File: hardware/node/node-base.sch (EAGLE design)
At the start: 19 parts, among them U1 INA322_DGK_8, U2 LMV551_DBV_5

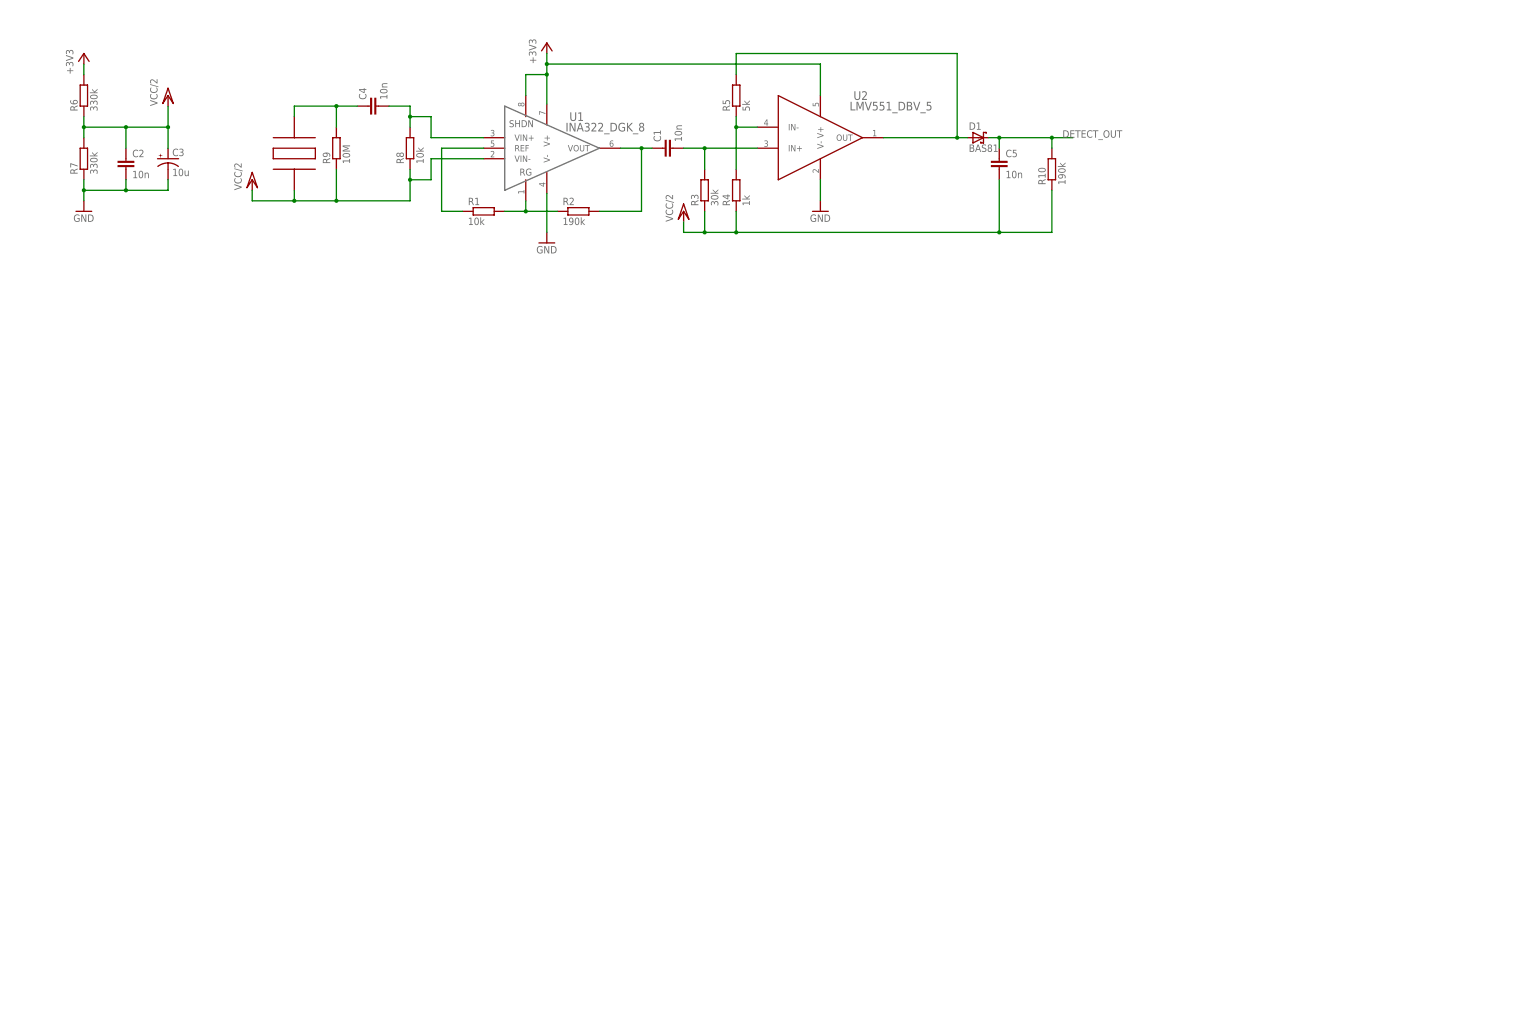
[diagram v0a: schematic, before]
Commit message: NODEHW: Added MCU power
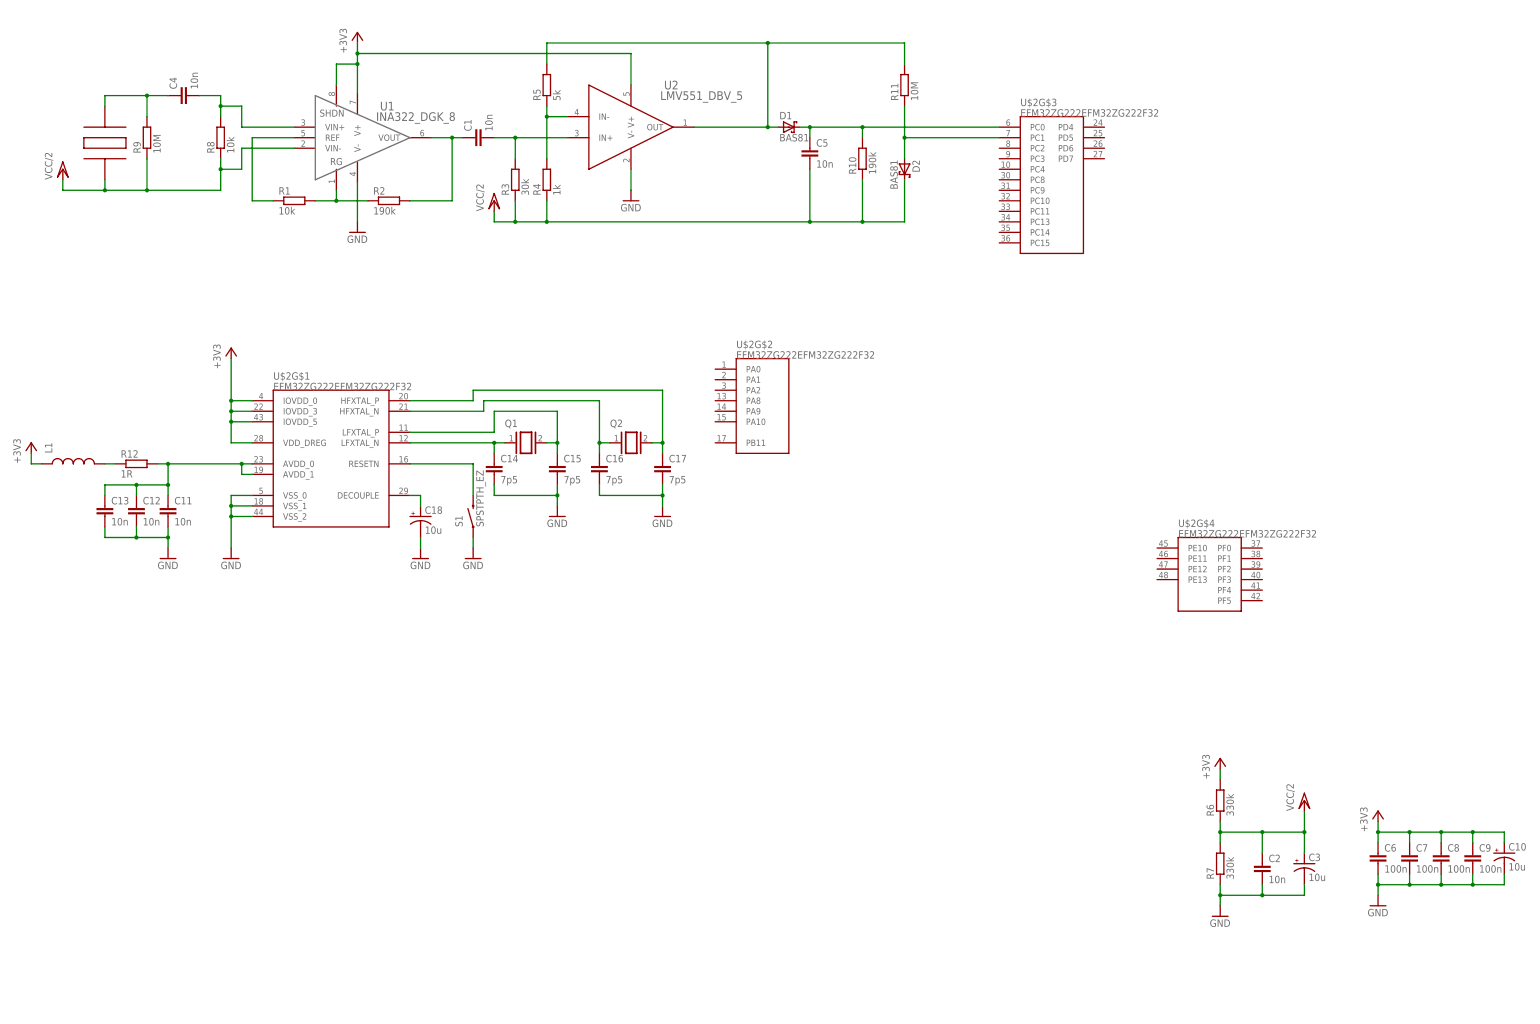
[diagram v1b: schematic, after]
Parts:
- added C10, C18: 10u, SparkFun-Capacitors:CAP_POLPTH2
- added C11, C12, C13: 10n, SparkFun-Capacitors:CAPPTH
- added C14, C15, C16, C17: 7p5, SparkFun-Capacitors:CAPPTH
- added C6, C7, C8, C9: 100n, SparkFun-Capacitors:CAPPTH
- added D2: BAS81, diode:SCHOTTKY-DIODECB417-15
- added L1: (no value), SparkFun-Passives:INDUCTOR0805
- added Q1, Q2: (no value), special:XTAL/S
- added R11: 10M, resistor:R-EU_0309/12
- added R12: 1R, resistor:R-EU_0309/12
- added S1: SPSTPTH_EZ, SparkFun-Electromechanical:SPSTPTH_EZ
- added U$2: EFM32ZG222EFM32ZG222F32, FullyCustom:EFM32ZG222EFM32ZG222F32
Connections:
- new net N$12: S1.2, U$2G$1.RESETN
- new net N$14: C14.1, Q1.1, U$2G$1.LFXTAL_N
- new net N$16: C15.1, Q1.2, U$2G$1.LFXTAL_P
- new net N$17: C16.1, Q2.1, U$2G$1.HFXTAL_N
- new net N$18: C17.1, Q2.2, U$2G$1.HFXTAL_P
- new net N$23: C18.+, U$2G$1.DECOUPLE
- new net N$3: D2.A, R11.1, U$2G$3.PC1
- new net N$6: L1.2, R12.1
- new net N$8: C11.1, C12.1, C13.1, R12.2, U$2G$1.AVDD_0, U$2G$1.AVDD_1
- net +3V3: now also C10.+, C6.1, C7.1, C8.1, C9.1, L1.1, U$2G$1.IOVDD_0, U$2G$1.IOVDD_3, U$2G$1.IOVDD_5, U$2G$1.VDD_DREG
- net DETECT_OUT: now also U$2G$3.PC0
- net GND: now also C10.-, C11.2, C12.2, C13.2, C14.2, C15.2, C16.2, C17.2, C18.-, C6.2, C7.2, C8.2, C9.2, S1.1, U$2G$1.VSS_0, U$2G$1.VSS_1, U$2G$1.VSS_2
- net N$2: now also R11.2
- net VCC/2: now also D2.C
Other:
- moved on the sheet: C1, C2, C3, C4, C5, D1, R1, R10, R2, R3, R4, R5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

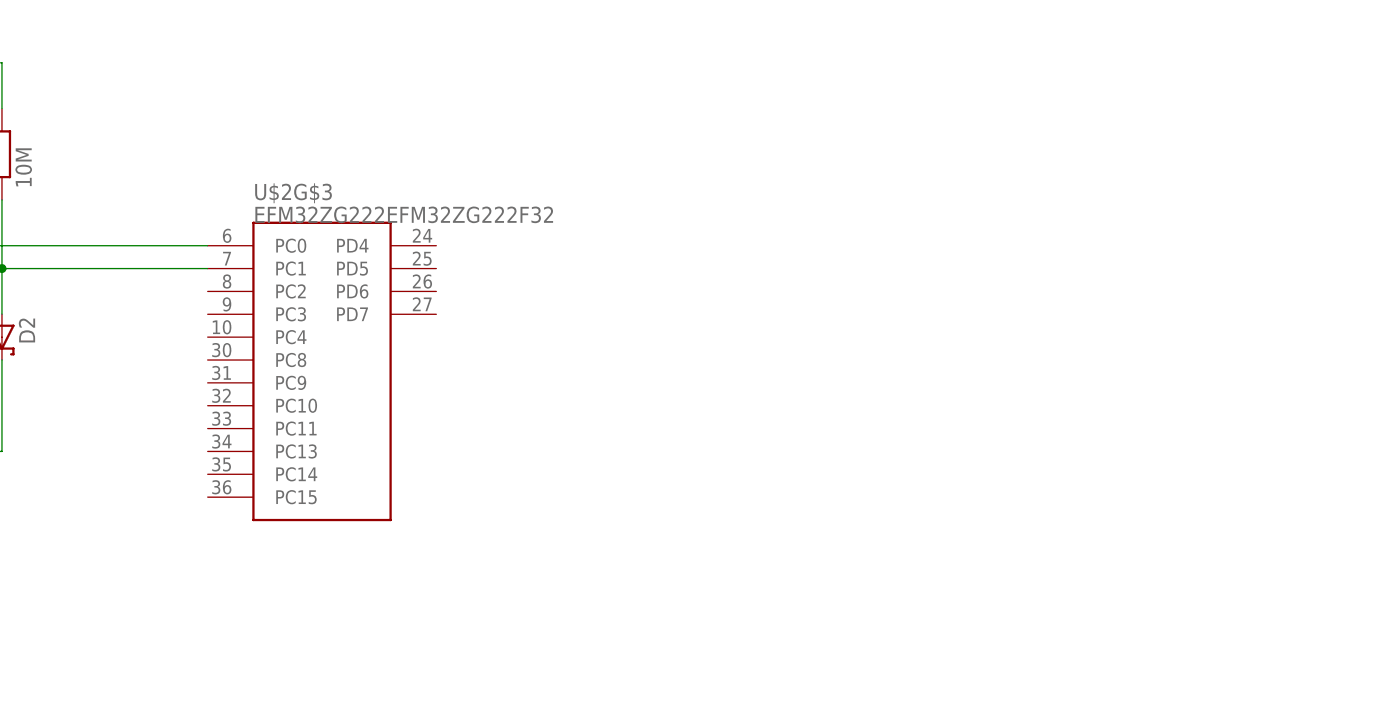
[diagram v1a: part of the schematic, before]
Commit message: NODE: Added radio
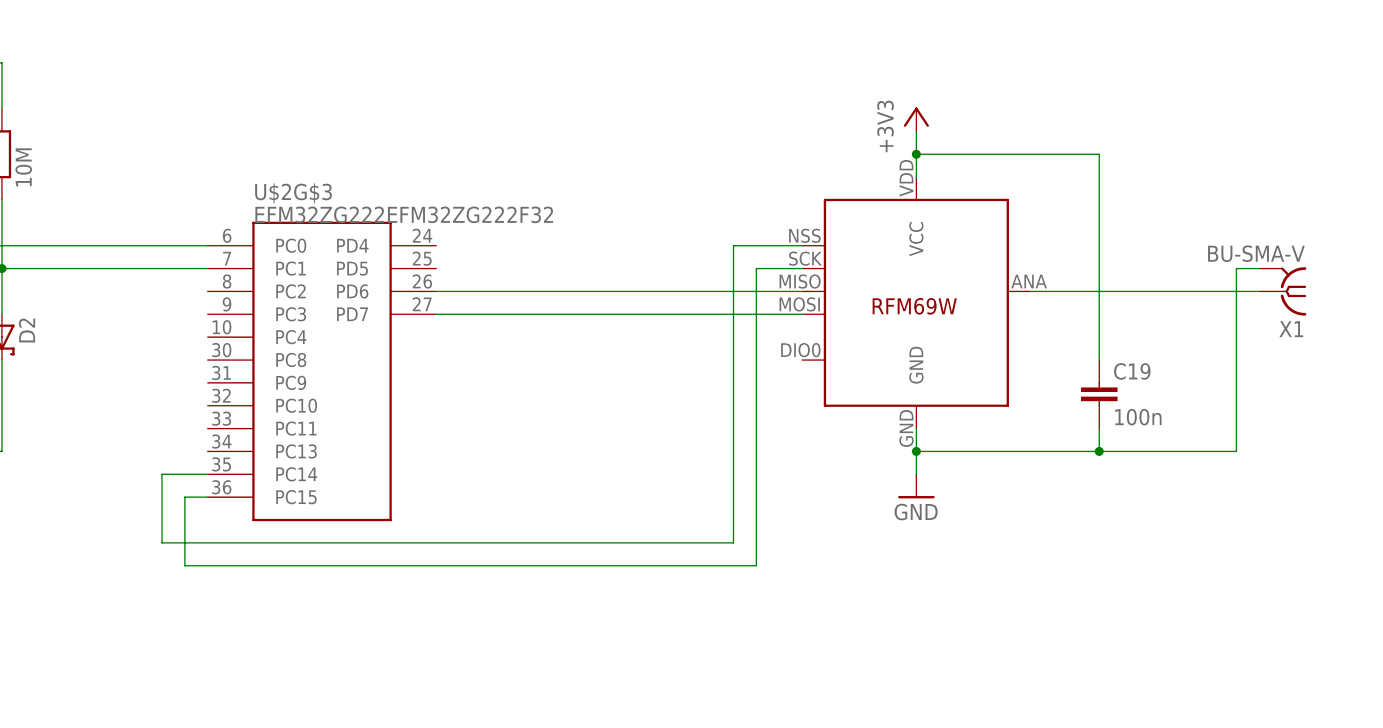
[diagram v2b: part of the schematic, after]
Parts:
- added C19: 100n, SparkFun-Capacitors:CAPPTH
- added U$3: RFM69, Moteino:RFM69
- added X1: BU-SMA-V, con-coax:BU-SMA-V
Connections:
- new net N$13: U$2G$3.PD6, U$3.MISO
- new net N$15: U$2G$3.PD7, U$3.MOSI
- new net N$19: U$2G$3.PC14, U$3.SEL
- new net N$20: U$2G$3.PC15, U$3.SCK
- new net N$22: U$3.ANT, X1.1
- net +3V3: now also C19.1, U$3.VCC
- net GND: now also C19.2, U$3.GND, X1.2
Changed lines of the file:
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@@
 <grid distance="0.1" unitdist="inch" unit="inch" style="lines" multiple="1" display="no" altdistance="0.01" altunitdist="inch" altunit="inch"/>
 <layers>
-<layer number="1" name="Top" color="4" fill="1" visible="yes" active="no"/>
-<layer number="16" name="Bottom" color="1" fill="1" visible="yes" active="no"/>
-<layer number="17" name="Pads" color="2" fill="1" visible="yes" active="no"/>
-<layer number="18" name="Vias" color="2" fill="1" visible="yes" active="no"/>
-<layer number="19" name="Unrouted" color="6" fill="1" visible="yes" active="no"/>
-<layer number="20" name="Dimension" color="15" fill="1" visible="yes" active="no"/>
-<layer number="21" name="tPlace" color="7" fill="1" visible="yes" active="no"/>
-<layer number="22" name="bPlace" color="7" fill="1" visible="yes" active="no"/>
-<layer number="23" name="tOrigins" color="15" fill="1" visible="yes" active="no"/>
-<layer number="24" name="bOrigins" color="15" fill="1" visible="yes" active="no"/>
-<layer number="25" name="tNames" color="7" fill="1" visible="yes" active="no"/>
-<layer number="26" name="bNames" color="7" fill="1" visible="yes" active="no"/>
-<layer number="27" name="tValues" color="7" fill="1" visible="yes" active="no"/>
-<layer number="28" name="bValues" color="7" fill="1" visible="yes" active="no"/>
+<layer number="1" name="Top" color="4" fill="1" visible="no" active="no"/>
+<layer number="16" name="Bottom" color="1" fill="1" visible="no" active="no"/>
+<layer number="17" name="Pads" color="2" fill="1" visible="no" active="no"/>
+<layer number="18" name="Vias" color="2" fill="1" visible="no" active="no"/>
+<layer number="19" name="Unrouted" color="6" fill="1" visible="no" active="no"/>
+<layer number="20" name="Dimension" color="15" fill="1" visible="no" active="no"/>
+<layer number="21" name="tPlace" color="7" fill="1" visible="no" active="no"/>
+<layer number="22" name="bPlace" color="7" fill="1" visible="no" active="no"/>
+<layer number="23" name="tOrigins" color="15" fill="1" visible="no" active="no"/>
+<layer number="24" name="bOrigins" color="15" fill="1" visible="no" active="no"/>
+<layer number="25" name="tNames" color="7" fill="1" visible="no" active="no"/>
+<layer number="26" name="bNames" color="7" fill="1" visible="no" active="no"/>
+<layer number="27" name="tValues" color="7" fill="1" visible="no" active="no"/>
+<layer number="28" name="bValues" color="7" fill="1" visible="no" active="no"/>
 <layer number="29" name="tStop" color="7" fill="3" visible="no" active="no"/>
 <layer number="30" name="bStop" color="7" fill="6" visible="no" active="no"/>
@@
 <layer number="35" name="tGlue" color="7" fill="4" visible="no" active="no"/>
 <layer number="36" name="bGlue" color="7" fill="5" visible="no" active="no"/>
-<layer number="37" name="tTest" color="7" fill="1" visible="yes" active="no"/>
-<layer number="38" name="bTest" color="7" fill="1" visible="yes" active="no"/>
+<layer number="37" name="tTest" color="7" fill="1" visible="no" active="no"/>
+<layer number="38" name="bTest" color="7" fill="1" visible="no" active="no"/>
 <layer number="39" name="tKeepout" color="4" fill="11" visible="no" active="no"/>
 <layer number="40" name="bKeepout" color="1" fill="11" visible="no" active="no"/>
@@
 <layer number="44" name="Drills" color="7" fill="1" visible="no" active="no"/>
 <layer number="45" name="Holes" color="7" fill="1" visible="no" active="no"/>
-<layer number="46" name="Milling" color="3" fill="1" visible="yes" active="no"/>
-<layer number="47" name="Measures" color="7" fill="1" visible="yes" active="no"/>
-<layer number="48" name="Document" color="7" fill="1" visible="yes" active="no"/>
-<layer number="49" name="Reference" color="7" fill="1" visible="yes" active="no"/>
-<layer number="50" name="dxf" color="7" fill="1" visible="yes" active="no"/>
-<layer number="51" name="tDocu" color="7" fill="1" visible="yes" active="no"/>
-<layer number="52" name="bDocu" color="7" fill="1" visible="yes" active="no"/>
-<layer number="53" name="tGND_GNDA" color="7" fill="9" visible="yes" active="no"/>
-<layer number="54" name="bGND_GNDA" color="1" fill="9" visible="yes" active="no"/>
-<layer number="56" name="wert" color="7" fill="1" visible="yes" active="no"/>
+<layer number="46" name="Milling" color="3" fill="1" visible="no" active="no"/>
+<layer number="47" name="Measures" color="7" fill="1" visible="no" active="no"/>
+<layer number="48" name="Document" color="7" fill="1" visible="no" active="no"/>
+<layer number="49" name="Reference" color="7" fill="1" visible="no" active="no"/>
+<layer number="50" name="dxf" color="7" fill="1" visible="no" active="no"/>
+<layer number="51" name="tDocu" color="7" fill="1" visible="no" active="no"/>
+<layer number="52" name="bDocu" color="7" fill="1" visible="no" active="no"/>
+<layer number="53" name="tGND_GNDA" color="7" fill="9" visible="no" active="no"/>
+<layer number="54" name="bGND_GNDA" color="1" fill="9" visible="no" active="no"/>
+<layer number="56" name="wert" color="7" fill="1" visible="no" active="no"/>
 <layer number="57" name="tCAD" color="7" fill="1" visible="no" active="no"/>
 <layer number="90" name="Modules" color="5" fill="1" visible="yes" active="yes"/>
@@
 <part name="S1" library="SparkFun-Electromechanical" deviceset="SPST" device="PTH_EZ"/>
 <part name="GND10" library="supply1" deviceset="GND" device=""/>
+<part name="U$3" library="Moteino" deviceset="RFM69" device=""/>
+<part name="+3V6" library="supply1" deviceset="+3V3" device=""/>
+<part name="GND12" library="supply1" deviceset="GND" device=""/>
+<part name="C19" library="SparkFun-Capacitors" deviceset="CAP" device="PTH" value="100n"/>
+<part name="X1" library="con-coax" deviceset="BU-SMA-V" device=""/>
 </parts>
 <sheets>
@@
 <instance part="S1" gate="G$1" x="116.84" y="127" rot="R90"/>
 <instance part="GND10" gate="1" x="116.84" y="116.84"/>
+<instance part="U$3" gate="G$1" x="322.58" y="213.36"/>
+<instance part="+3V6" gate="G$1" x="322.58" y="236.22"/>
+<instance part="GND12" gate="1" x="322.58" y="193.04"/>
+<instance part="C19" gate="G$1" x="342.9" y="203.2"/>
+<instance part="X1" gate="G$1" x="363.22" y="215.9" rot="R180"/>
 </instances>
 <busses>
@@
 <pinref part="GND10" gate="1" pin="GND"/>
 <wire x1="116.84" y1="121.92" x2="116.84" y2="119.38" width="0.1524" layer="91"/>
+</segment>
+<segment>
+<pinref part="U$3" gate="G$1" pin="GND"/>
+<pinref part="GND12" gate="1" pin="GND"/>
+<wire x1="322.58" y1="200.66" x2="322.58" y2="198.12" width="0.1524" layer="91"/>
+<wire x1="322.58" y1="198.12" x2="322.58" y2="195.58" width="0.1524" layer="91"/>
+<wire x1="322.58" y1="198.12" x2="342.9" y2="198.12" width="0.1524" layer="91"/>
+<junction x="322.58" y="198.12"/>
+<pinref part="C19" gate="G$1" pin="2"/>
+<wire x1="342.9" y1="198.12" x2="342.9" y2="200.66" width="0.1524" layer="91"/>
+<pinref part="X1" gate="G$1" pin="2"/>
+<wire x1="360.68" y1="218.44" x2="358.14" y2="218.44" width="0.1524" layer="91"/>
+<wire x1="358.14" y1="218.44" x2="358.14" y2="198.12" width="0.1524" layer="91"/>
+<wire x1="358.14" y1="198.12" x2="342.9" y2="198.12" width="0.1524" layer="91"/>
+<junction x="342.9" y="198.12"/>
 </segment>
 </net>
@@
 <wire x1="10.16" y1="139.7" x2="10.16" y2="142.24" width="0.1524" layer="91"/>
 </segment>
+<segment>
+<pinref part="+3V6" gate="G$1" pin="+3V3"/>
+<pinref part="U$3" gate="G$1" pin="VCC"/>
+<wire x1="322.58" y1="233.68" x2="322.58" y2="231.14" width="0.1524" layer="91"/>
+<pinref part="C19" gate="G$1" pin="1"/>
+<wire x1="322.58" y1="231.14" x2="322.58" y2="228.6" width="0.1524" layer="91"/>
+<wire x1="342.9" y1="208.28" x2="342.9" y2="231.14" width="0.1524" layer="91"/>
+<wire x1="342.9" y1="231.14" x2="322.58" y2="231.14" width="0.1524" layer="91"/>
+<junction x="322.58" y="231.14"/>
+</segment>
 </net>
 <net name="N$3" class="0">
@@
 </segment>
 </net>
+<net name="N$13" class="0">
+<segment>
+<pinref part="U$2" gate="G$3" pin="PD6"/>
+<pinref part="U$3" gate="G$1" pin="MISO"/>
+<wire x1="269.24" y1="215.9" x2="309.88" y2="215.9" width="0.1524" layer="91"/>
+</segment>
+</net>
+<net name="N$15" class="0">
+<segment>
+<pinref part="U$3" gate="G$1" pin="MOSI"/>
+<pinref part="U$2" gate="G$3" pin="PD7"/>
+<wire x1="309.88" y1="213.36" x2="269.24" y2="213.36" width="0.1524" layer="91"/>
+</segment>
+</net>
+<net name="N$19" class="0">
+<segment>
+<pinref part="U$2" gate="G$3" pin="PC14"/>
+<wire x1="243.84" y1="195.58" x2="238.76" y2="195.58" width="0.1524" layer="91"/>
+<wire x1="238.76" y1="195.58" x2="238.76" y2="187.96" width="0.1524" layer="91"/>
+<wire x1="238.76" y1="187.96" x2="302.26" y2="187.96" width="0.1524" layer="91"/>
+<wire x1="302.26" y1="187.96" x2="302.26" y2="220.98" width="0.1524" layer="91"/>
+<pinref part="U$3" gate="G$1" pin="SEL"/>
+<wire x1="302.26" y1="220.98" x2="309.88" y2="220.98" width="0.1524" layer="91"/>
+</segment>
+</net>
+<net name="N$20" class="0">
+<segment>
+<pinref part="U$2" gate="G$3" pin="PC15"/>
+<wire x1="243.84" y1="193.04" x2="241.3" y2="193.04" width="0.1524" layer="91"/>
+<wire x1="241.3" y1="193.04" x2="241.3" y2="185.42" width="0.1524" layer="91"/>
+<wire x1="241.3" y1="185.42" x2="304.8" y2="185.42" width="0.1524" layer="91"/>
+<wire x1="304.8" y1="185.42" x2="304.8" y2="218.44" width="0.1524" layer="91"/>
+<pinref part="U$3" gate="G$1" pin="SCK"/>
+<wire x1="304.8" y1="218.44" x2="309.88" y2="218.44" width="0.1524" layer="91"/>
+</segment>
+</net>
+<net name="N$22" class="0">
+<segment>
+<pinref part="X1" gate="G$1" pin="1"/>
+<pinref part="U$3" gate="G$1" pin="ANT"/>
+<wire x1="360.68" y1="215.9" x2="335.28" y2="215.9" width="0.1524" layer="91"/>
+</segment>
+</net>
